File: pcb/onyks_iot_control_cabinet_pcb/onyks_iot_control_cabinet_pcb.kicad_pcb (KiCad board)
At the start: 2 copper layers, 37 parts, among them J1 Conn_01x02_Socket, J2 Conn_01x06_Socket, J3 Screw_Terminal_01x02, J4 Jack-DC, J5 Conn_01x09_Socket, J6 Conn_01x04_Socket, J7 Screw_Terminal_01x02, J8 Conn_01x04_Socket, J9 Conn_01x02_Socket, Q1 SQ4940CEY-T1_GE3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

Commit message: PCB's update
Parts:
- removed J6: Conn_01x04_Socket, Connector_PinHeader_2.54mm:PinHeader_1x04_P2.54mm_Vertical
- added J10: Conn_02x05_Odd_Even, Connector_PinHeader_2.54mm:PinHeader_2x05_P2.54mm_Vertical, F.Cu at (52.2, 45.3)
- J8: value Conn_01x04_Socket -> Conn_01x06_Pin; footprint Connector_PinHeader_2.54mm:PinHeader_1x04_P2.54mm_Vertical -> Connector_PinHeader_2.54mm:PinHeader_1x06_P2.54mm_Vertical
- SW1, SW2, SW3: footprint Button_Switch_SMD:SW_Push_SPST_NO_Alps_SKRK -> Button_Switch_SMD:SW_Tactile_SPST_NO_Straight_CK_PTS636Sx25SMTRLFS
- moved J1 174.1 mm to (52.5, 64.5), turned to 0 degrees
- moved C5 170.5 mm to (59.0, 67.6), turned to 90 degrees
- moved SW3 165.5 mm to (67.1, 66.6), turned to 180 degrees
- moved R3 150.0 mm to (62.5, 79.8)
- moved Q3 149.3 mm to (62.5, 85.6)
- moved G*** 148.5 mm to (99.0, 35.0)
- moved Q4 146.3 mm to (62.5, 76.4), turned to 180 degrees
- moved R4 145.5 mm to (62.4, 82.4), turned to 180 degrees
- moved C1 144.5 mm to (61.7, 35.5), turned to -90 degrees
- moved U1 144.2 mm to (75.1, 42.1)
- moved SW2 143.9 mm to (85.0, 89.1), turned to 0 degrees
- moved C2 141.3 mm to (60.2, 40.9), turned to -90 degrees
- moved J5 140.9 mm to (90.2, 46.7)
- moved C4 140.4 mm to (84.9, 94.1)
- moved BZ1 138.6 mm to (104.2, 86.7)
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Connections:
- J8 pad 1: JTAG_MTDI -> RTS
- J8 pad 2: JTAG_MTCK -> DTR
- J8 pad 3: JTAG_MTMS -> MCU_RX_PROG
- J8 pad 4: JTAG_MTDO -> MCU_TX_PROG
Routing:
- net +3.3V: track 92.8 -> 0.00 mm
- net MCU_TX_PROG: track 23.9 -> 69.4 mm, vias 0 -> 3
- net MCU_RX_PROG: track 24.8 -> 66.6 mm, vias 2 -> 5
- net GND: track 2.98 -> 44.7 mm, vias 7 -> 24
- net Net-(D1-DIN): track 17.3 -> 45.8 mm
- net MCU_RESET: track 73.6 -> 95.0 mm, vias 4 -> 3
- net DTR: track 35.2 -> 13.8 mm, vias 2 -> 0
- net BUZZER_SWITCH: track 20.1 -> 38.3 mm
- net RTS: track 28.2 -> 12.4 mm, vias 4 -> 0
- net Net-(BZ1--_2): track 25.3 -> 11.6 mm
- net LOCK_SWITCH: track 31.2 -> 44.2 mm
- net LOCK_MCU_MANUAL_OPEN: track 40.9 -> 51.7 mm, vias 1 -> 2
- net FREE_GPIO_3: track 26.3 -> 15.8 mm, vias 4 -> 1
- net FREE_GPIO_2: track 20.3 -> 10.1 mm, vias 3 -> 0
- net Net-(U2-SW): track 6.60 -> 15.8 mm
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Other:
- board outline added: 80 x 90 mm
- board text added: "+"
- board text added: "-"
- board text added: "1"
- board text added: "2"
- board text added: "3"
- board text added: "3.3V"
- board text added: "4"
- board text added: "5"
- board text added: "6"
- board text added: "7"
- board text added: "8"
- board text added: "9"
- board text added: "BOOT"
- board text added: "DTR"
- board text added: "GND"
- board text added: "GPIOs"
- board text added: "IN"
- board text added: "IRQ"
- board text added: "JTAG"
- board text added: "LED"
- board text added: "LOCK I/O"
- board text added: "MANUALL OPEN"
- board text added: "MISO"
- board text added: "MOSI"
- board text added: "MTCK"
- board text added: "MTDI"
- board text added: "MTDO"
- board text added: "MTMS"
- board text added: "NFC"
- board text added: "PROGRAMMER"
- board text added: "RESET"
- board text added: "RST"
- board text added: "RTS"
- board text added: "RX"
- board text added: "TX"

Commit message: Minor corrections/Rules
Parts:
- moved C2 3.29 mm to (61.9, 38.1), turned to 180 degrees
- moved C1 0.83 mm to (62.5, 35.6), turned to 180 degrees
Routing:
- net V_IN: track 0.00 -> 9.94 mm, vias 0 -> 2
- net GND: track 44.7 -> 48.0 mm, vias 24 -> 25

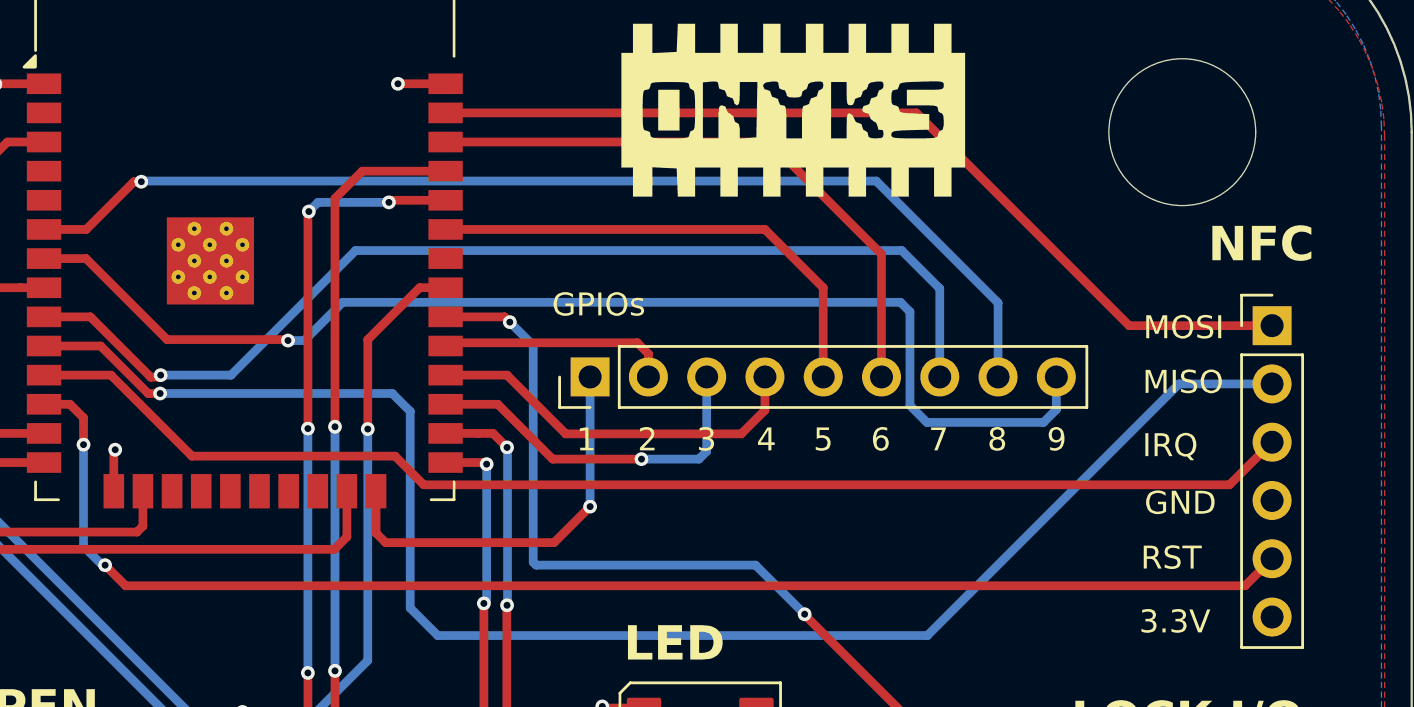
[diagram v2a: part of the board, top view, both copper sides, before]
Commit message: Patching GND for Free GPIO Connections
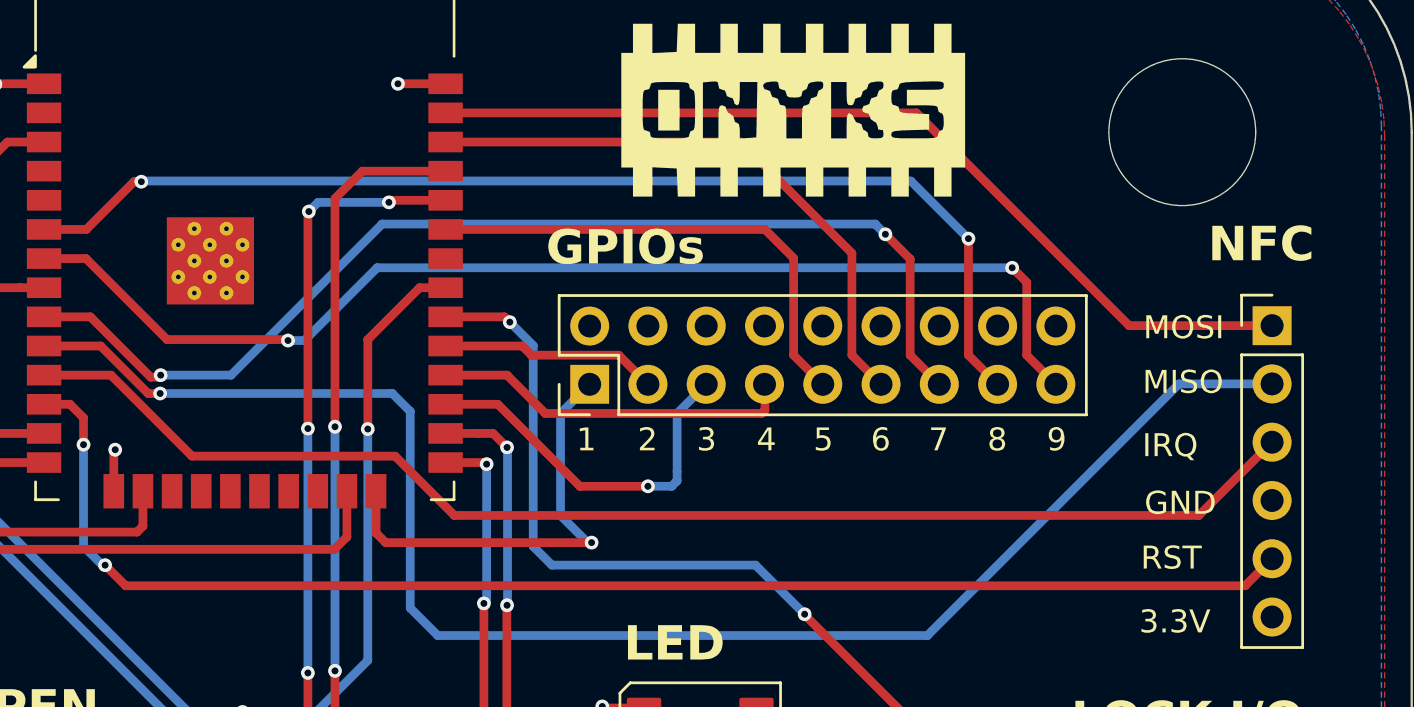
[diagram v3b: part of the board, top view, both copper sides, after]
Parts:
- removed J5: Conn_01x09_Socket, Connector_PinHeader_2.54mm:PinHeader_1x09_P2.54mm_Vertical
- added J6: Conn_02x09_Odd_Even, Connector_PinHeader_2.54mm:PinHeader_2x09_P2.54mm_Vertical, F.Cu at (90.2, 47.0)
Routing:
- net FREE_GPIO_1: track 17.6 -> 19.5 mm
- net FREE_GPIO_9: track 52.5 -> 50.9 mm, vias 1 -> 2
- net FREE_GPIO_7: track 47.0 -> 48.2 mm, vias 1 -> 2
- net FREE_GPIO_8: track 47.9 -> 49.1 mm, vias 1 -> 2
- net NFC_IRQ: track 56.3 -> 57.4 mm
- net FREE_GPIO_4: track 16.9 -> 16.1 mm
- net FREE_GPIO_3: track 15.8 -> 16.4 mm

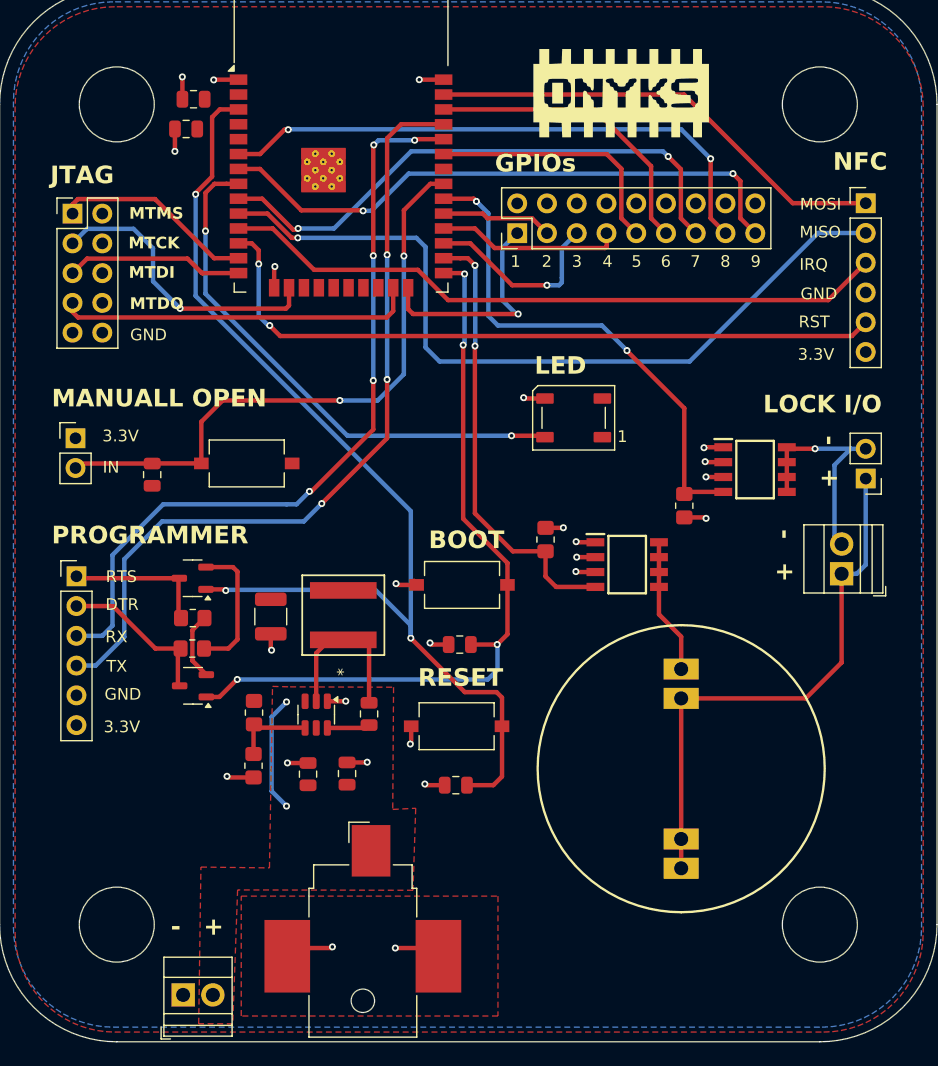
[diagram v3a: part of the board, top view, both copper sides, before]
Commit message: Add new rules, change JTAG and VCC polygon plane
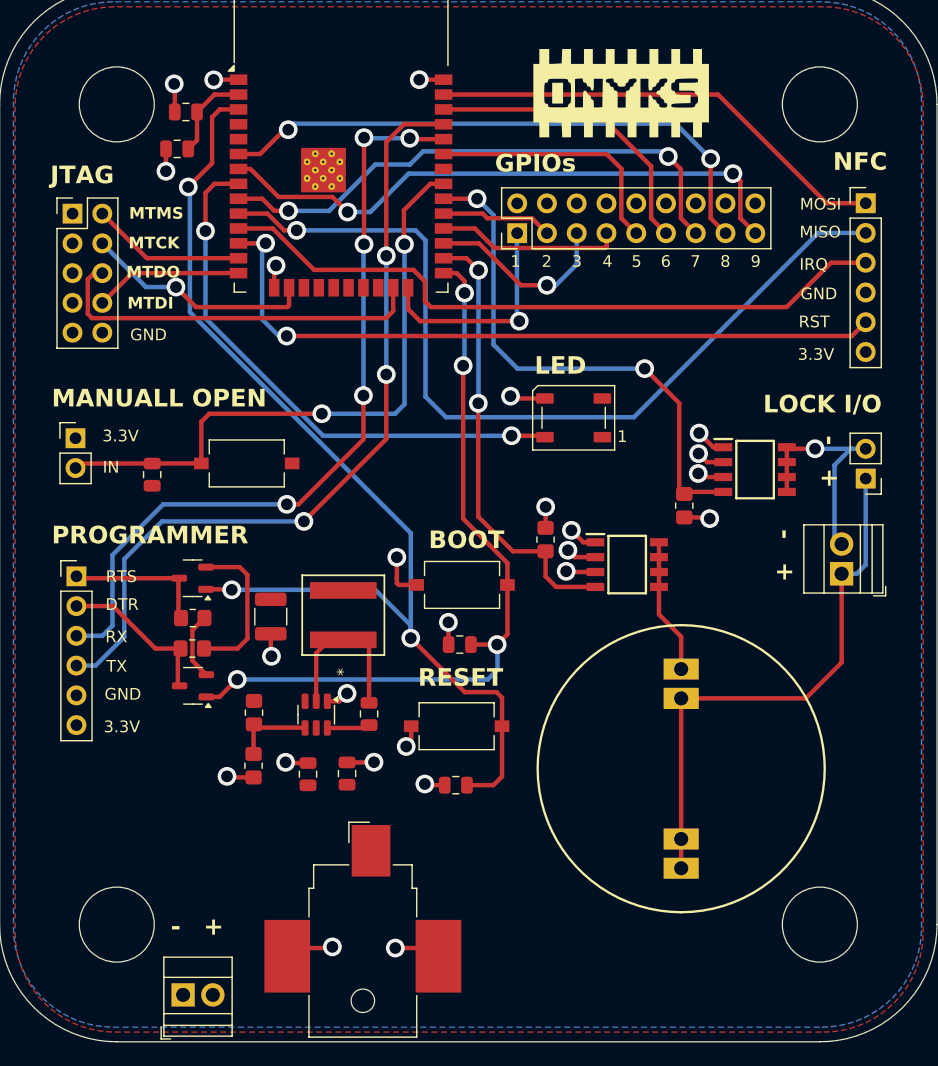
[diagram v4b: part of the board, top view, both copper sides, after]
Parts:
- Q1, Q2: value SQ4940CEY-T1_GE3 -> SQ4050EY-T1_GE3
- moved C2 1.86 mm to (61.1, 39.8)
- moved C1 1.27 mm to (61.9, 36.6)
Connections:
- J10 pad 1: JTAG_MTMS -> unconnected-(J10-Pin_1-Pad1)
- J10 pad 2: unconnected-(J10-Pin_2-Pad2) -> JTAG_MTMS
- J10 pad 3: JTAG_MTCK -> GND
- J10 pad 4: unconnected-(J10-Pin_4-Pad4) -> JTAG_MTCK
- J10 pad 5: JTAG_MTDI -> GND
- J10 pad 6: unconnected-(J10-Pin_6-Pad6) -> JTAG_MTDO
- J10 pad 7: JTAG_MTDO -> GND
- J10 pad 8: unconnected-(J10-Pin_8-Pad8) -> JTAG_MTDI
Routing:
- net GND: track 48.0 -> 61.4 mm
- net V_IN: track 9.94 -> 0.00 mm, vias 2 -> 0
- net +3.3V: track 0.00 -> 7.62 mm
- net NFC_MISO: track 68.3 -> 75.1 mm
- net JTAG_MTCK: track 25.1 -> 19.8 mm
- net JTAG_MTMS: track 17.2 -> 13.2 mm
- net JTAG_MTDI: track 15.2 -> 12.7 mm
- net JTAG_MTDO: track 31.2 -> 32.9 mm
- net LOCK_MCU_MANUAL_OPEN: track 51.7 -> 53.3 mm
- net Net-(Q4-B): track 11.8 -> 13.3 mm
- net NFC_IRQ: track 57.4 -> 58.9 mm
- net LOCK_SWITCH: track 43.8 -> 45.1 mm
- net FREE_GPIO_7: track 48.2 -> 46.9 mm
- net Net-(D1-DIN): track 45.8 -> 47.0 mm
- net MCU_RX_PROG: track 66.6 -> 67.6 mm
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- removed copper zone on F.Cu, net +3.3V
- removed copper zone on F.Cu, net V_IN

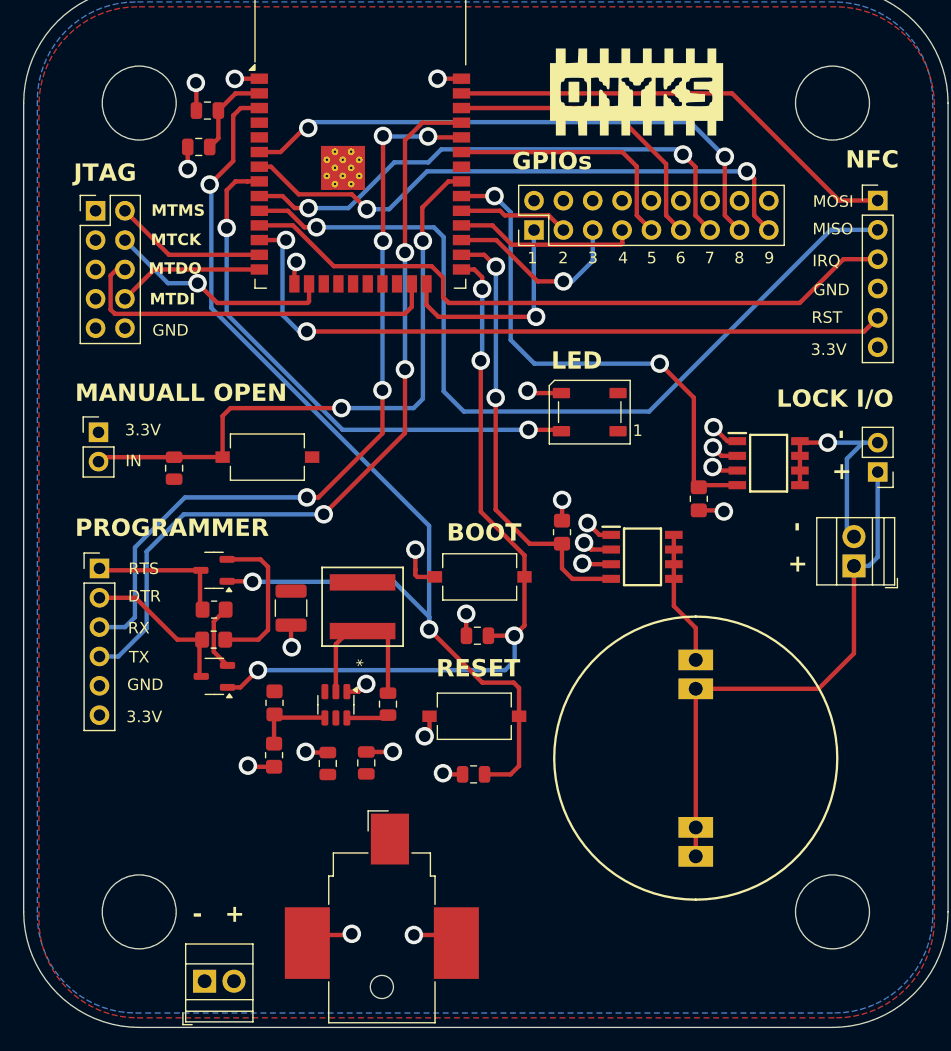
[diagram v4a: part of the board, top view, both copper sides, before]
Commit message: Changed VCC polygon into GND polygon, VCC traces added
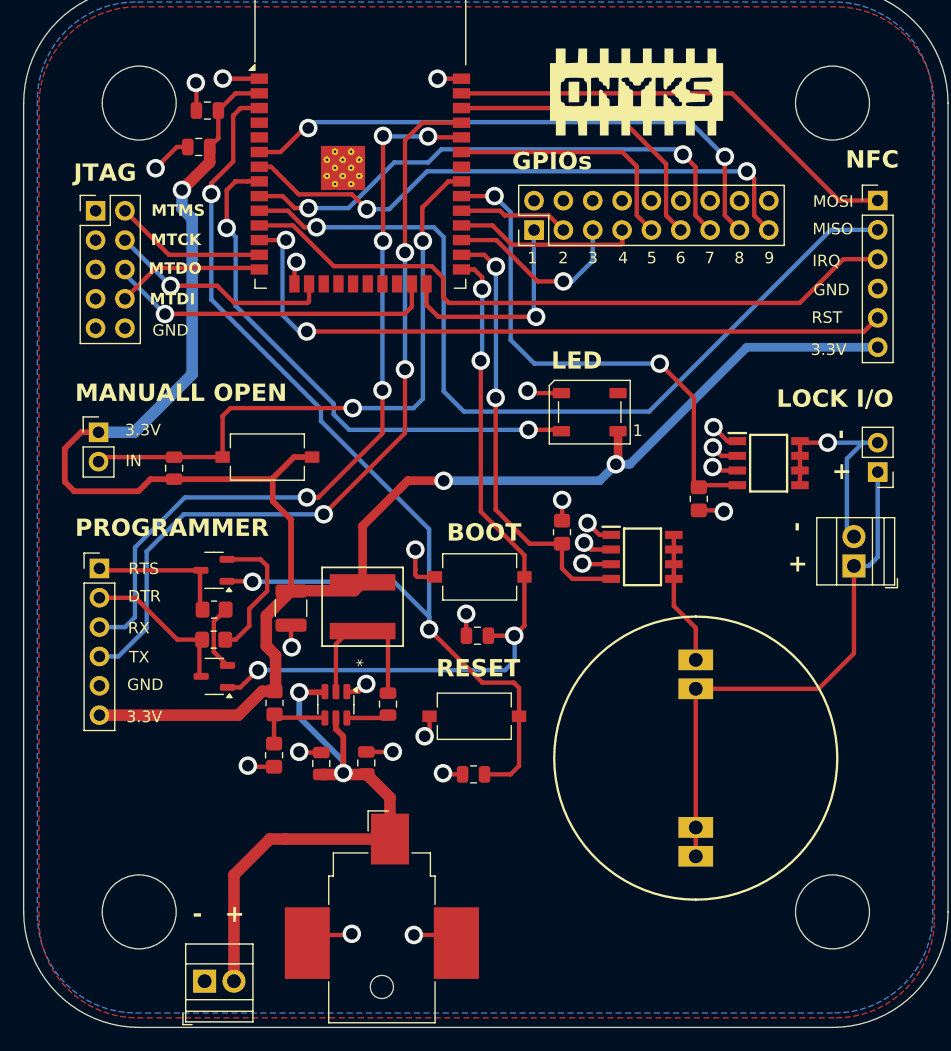
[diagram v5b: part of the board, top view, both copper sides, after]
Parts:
- moved C6 0.56 mm to (71.8, 93.2)
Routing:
- net +3.3V: track 7.62 -> 169.9 mm, vias 0 -> 3
- net V_IN: track 0.00 -> 50.4 mm, vias 0 -> 2
- net JTAG_MTDO: track 32.9 -> 28.9 mm, vias 0 -> 1
- net GND: track 61.4 -> 64.1 mm
- net Net-(Q4-B): track 13.3 -> 12.1 mm
